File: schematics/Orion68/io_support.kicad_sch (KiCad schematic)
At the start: 2 parts, among them J24 Euro96pin, U34 GAL20V8

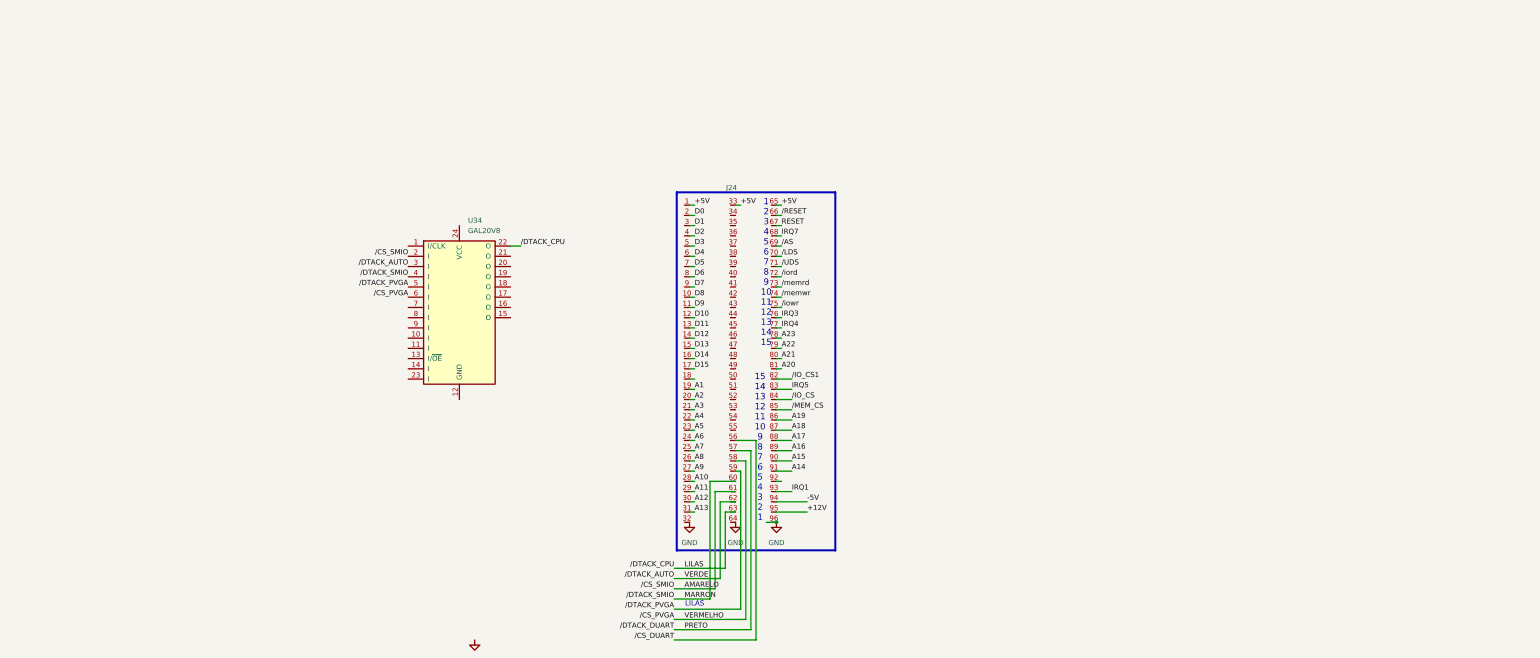
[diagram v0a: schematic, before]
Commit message: 2026-09-27: implemented and tested Orionide board
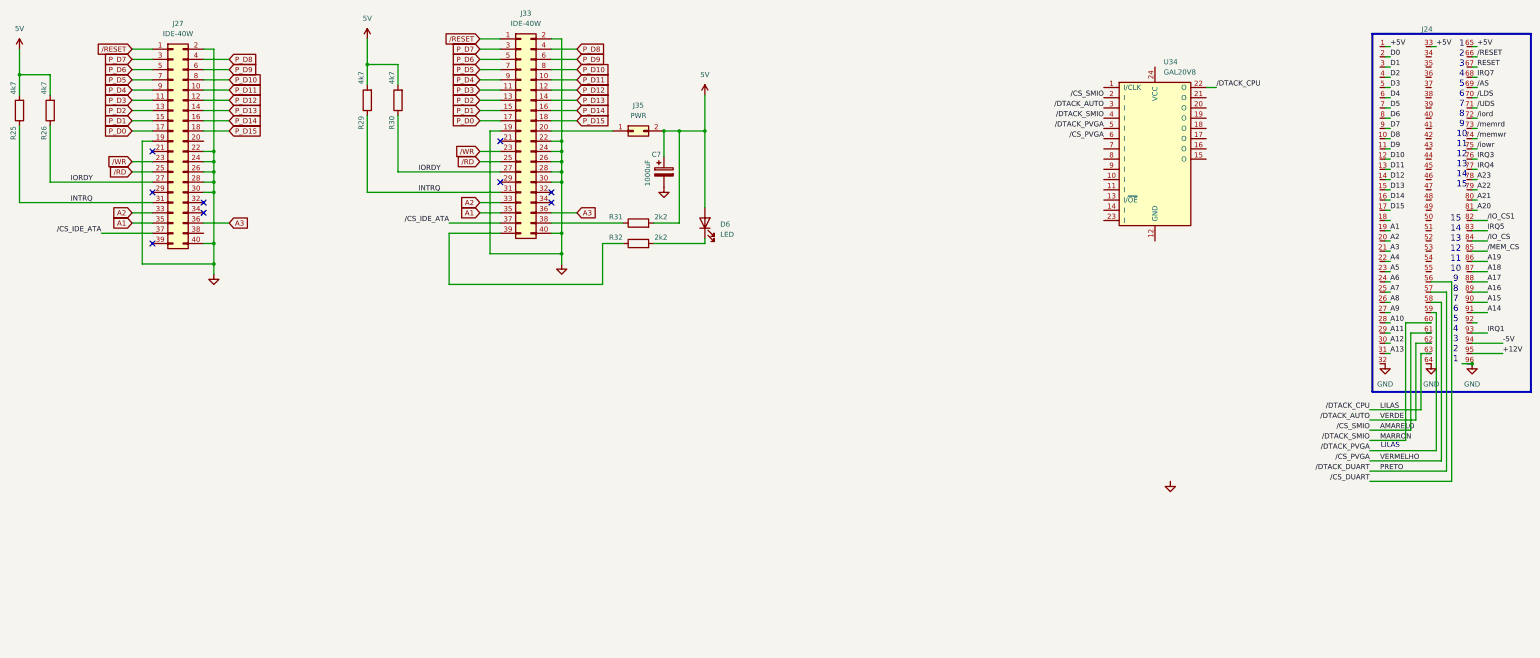
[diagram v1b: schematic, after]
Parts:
- added C7: 1000uF, symbol Device:C_Polarized
- added D6: LED, symbol Device:LED
- added J27, J33: IDE-40W, symbol Connector_Generic:Conn_02x20_Odd_Even
- added J35: PWR, symbol Connector_Generic:Conn_02x01
- added R25, R26, R29, R30: 4k7, symbol Device:R
- added R31, R32: 2k2, symbol Device:R
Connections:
- net A1: now also J27.35 (Pin_35), J33.35 (Pin_35)
- net A2: now also J27.33 (Pin_33), J33.33 (Pin_33)
- net A3: now also J27.36 (Pin_36), J33.36 (Pin_36)
- net GND: now also C7.2, J27.19 (Pin_19), J27.2 (Pin_2), J27.22 (Pin_22), J27.24 (Pin_24), J27.26 (Pin_26), J27.28 (Pin_28), J27.30 (Pin_30), J27.40 (Pin_40), J33.19 (Pin_19), J33.2 (Pin_2), J33.22 (Pin_22), J33.24 (Pin_24), J33.26 (Pin_26), J33.28 (Pin_28), J33.30 (Pin_30), J33.40 (Pin_40)
- net /RESET: now also J27.1 (Pin_1), J33.1 (Pin_1)
- new net: J33.20 (Pin_20), J35.1 (Pin_1)
- new net: D6.1 (K), R32.2
- new net: J33.38 (Pin_38), R31.1
- new net: J33.39 (Pin_39), R32.1
- new net 5V: C7.1, D6.2 (A), J35.2 (Pin_2), R25.2, R26.2, R29.2, R30.2, R31.2
- new net INTRQ: J27.31 (Pin_31), J33.31 (Pin_31), R25.1, R29.1
- new net IORDY: J27.27 (Pin_27), J33.27 (Pin_27), R26.1, R30.1
- new net P_D0: J27.17 (Pin_17), J33.17 (Pin_17)
- new net P_D1: J27.15 (Pin_15), J33.15 (Pin_15)
- new net P_D10: J27.8 (Pin_8), J33.8 (Pin_8)
- new net P_D11: J27.10 (Pin_10), J33.10 (Pin_10)
- new net P_D12: J27.12 (Pin_12), J33.12 (Pin_12)
- new net P_D13: J27.14 (Pin_14), J33.14 (Pin_14)
- new net P_D14: J27.16 (Pin_16), J33.16 (Pin_16)
- new net P_D15: J27.18 (Pin_18), J33.18 (Pin_18)
- new net P_D2: J27.13 (Pin_13), J33.13 (Pin_13)
- new net P_D3: J27.11 (Pin_11), J33.11 (Pin_11)
- new net P_D4: J27.9 (Pin_9), J33.9 (Pin_9)
- new net P_D5: J27.7 (Pin_7), J33.7 (Pin_7)
- new net P_D6: J27.5 (Pin_5), J33.5 (Pin_5)
- new net P_D7: J27.3 (Pin_3), J33.3 (Pin_3)
- new net P_D8: J27.4 (Pin_4), J33.4 (Pin_4)
- new net P_D9: J27.6 (Pin_6), J33.6 (Pin_6)
- new net /CS_IDE_ATA: J27.37 (Pin_37), J33.37 (Pin_37)
- new net /RD: J27.25 (Pin_25), J33.25 (Pin_25)
- new net /WR: J27.23 (Pin_23), J33.23 (Pin_23)
- no-connect marks 0 -> 9
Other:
- moved on the sheet: J24, U34

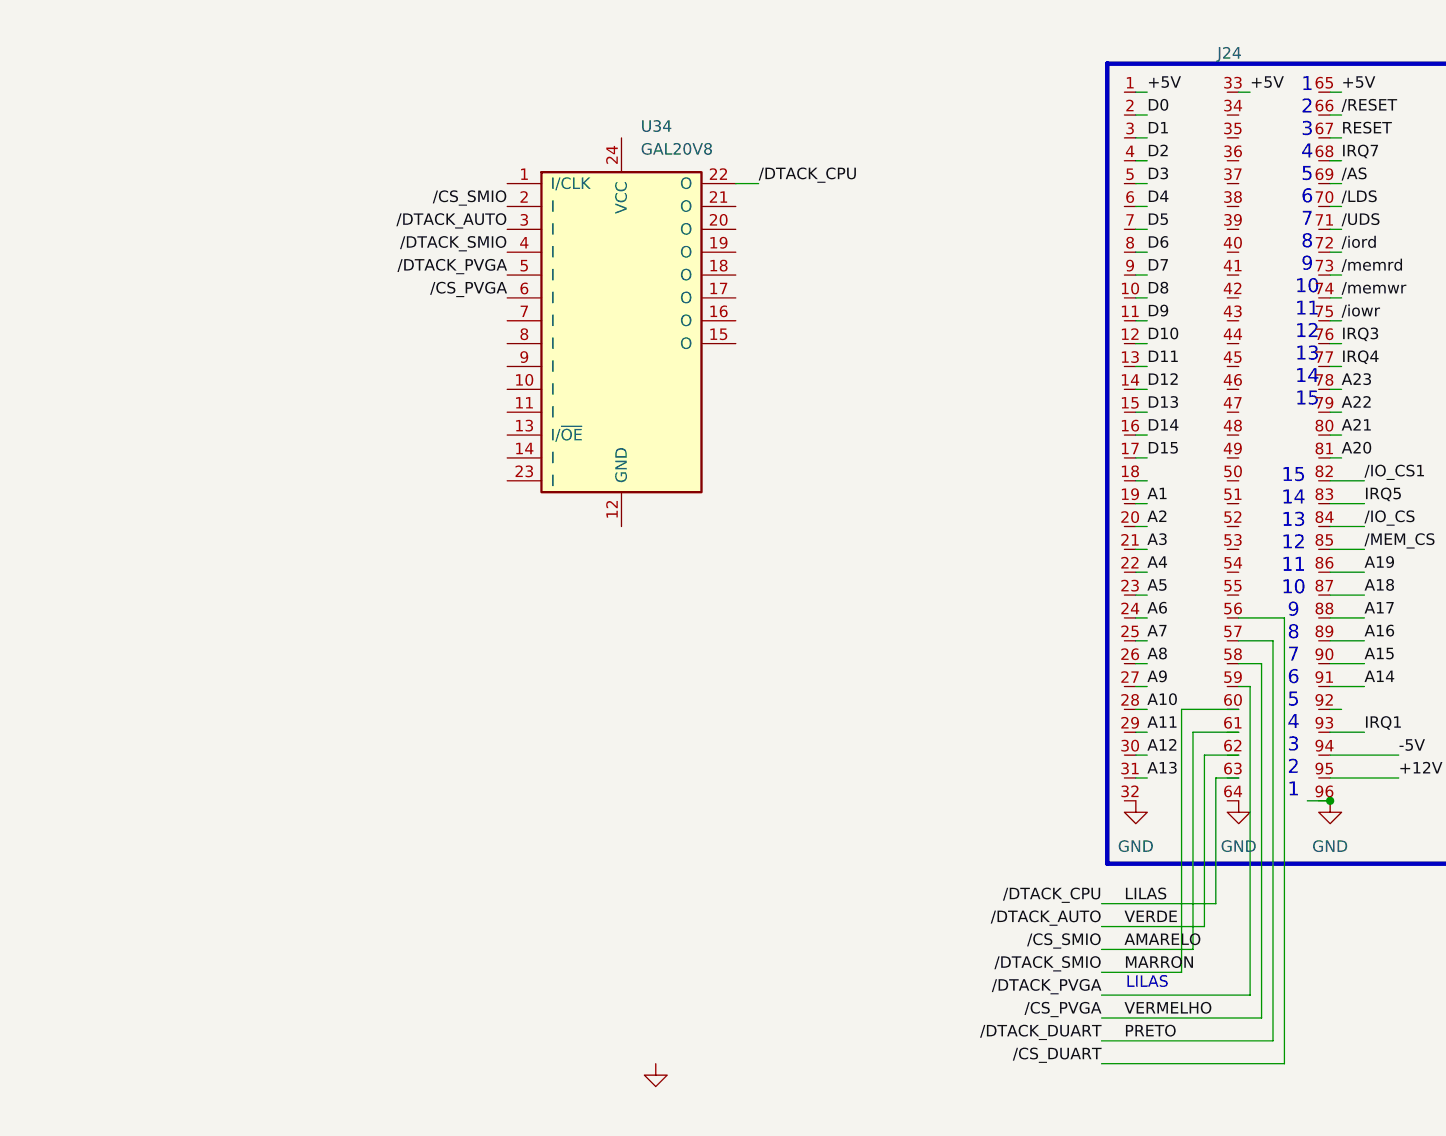
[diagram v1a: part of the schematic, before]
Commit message: 2026-10-03: CHANGED FROM PIGBACK BOARD to 74hc138 + 74hc4078
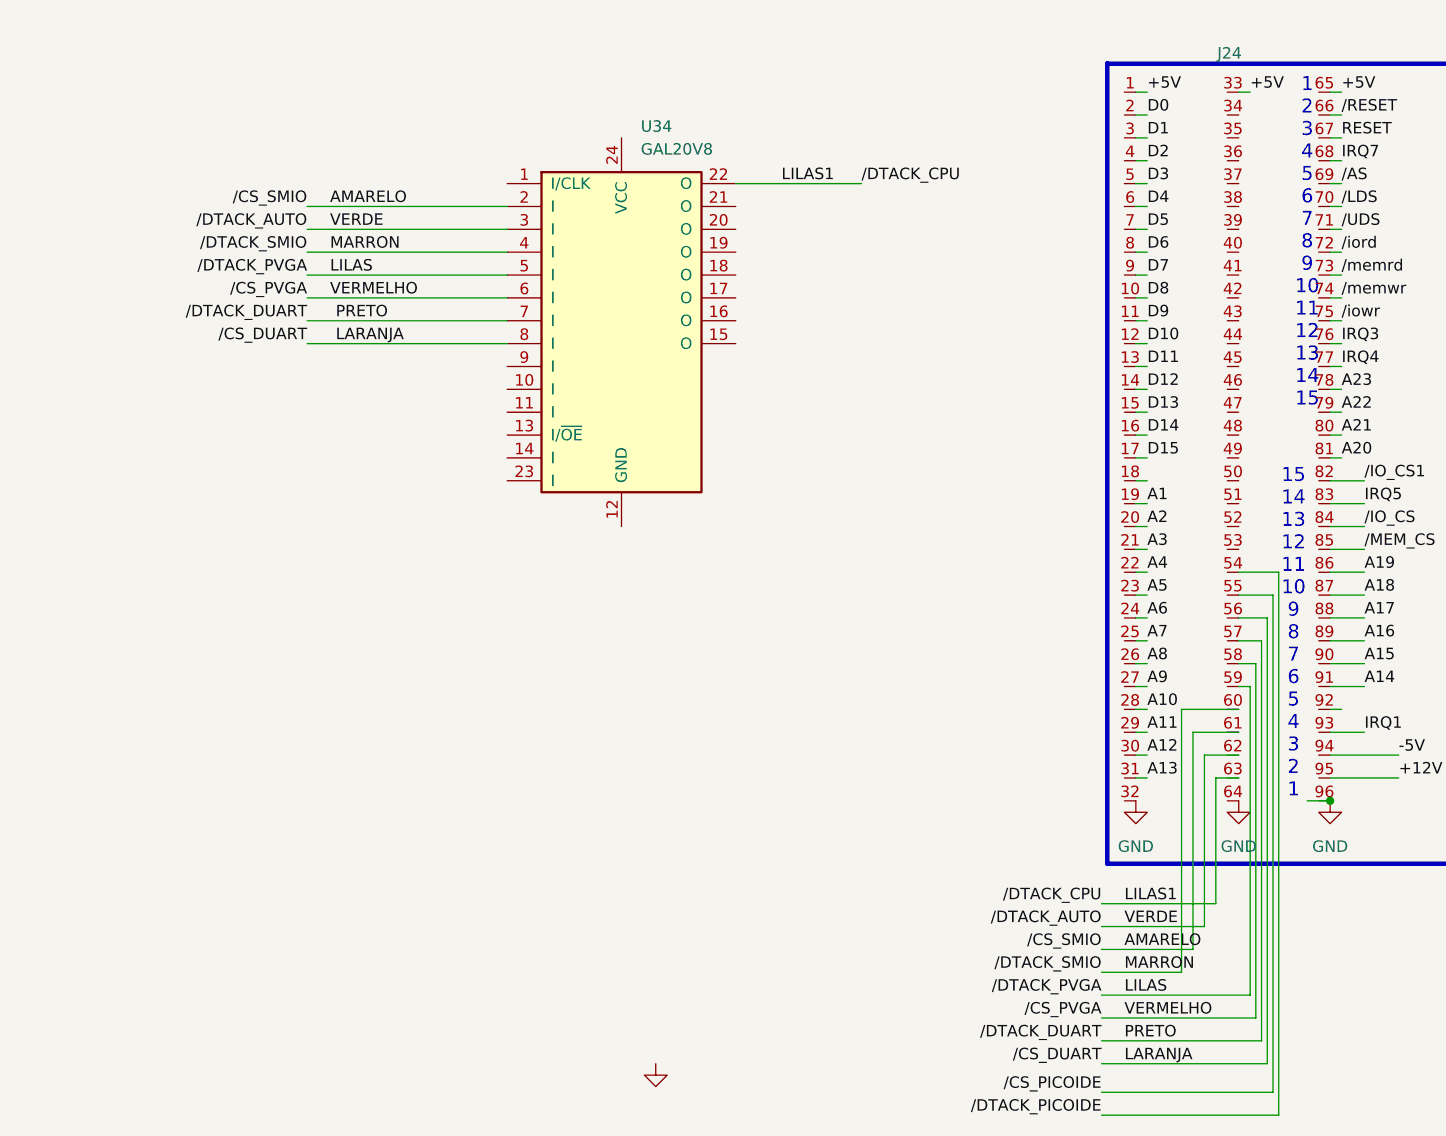
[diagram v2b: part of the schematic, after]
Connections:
- net /CS_DUART is gone; now on net LARANJA: J24.56
- net /DTACK_PVGA is gone; now on net LILAS: J24.59, U34.5 (I)
- net LILAS: no longer J24.63, U34.22 (O)
- net PRETO: now also U34.7 (I)
- net /DTACK_PICOIDE: now reaches J24.54
- net /CS_PICOIDE: now reaches J24.55
- net LARANJA: now reaches U34.8 (I)
- new net LILAS1: J24.63, U34.22 (O)
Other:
- note removed: "LILAS"
